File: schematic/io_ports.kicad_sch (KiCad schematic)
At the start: 4 parts, among them J1 Cartridge Port, J2 Expansion Port

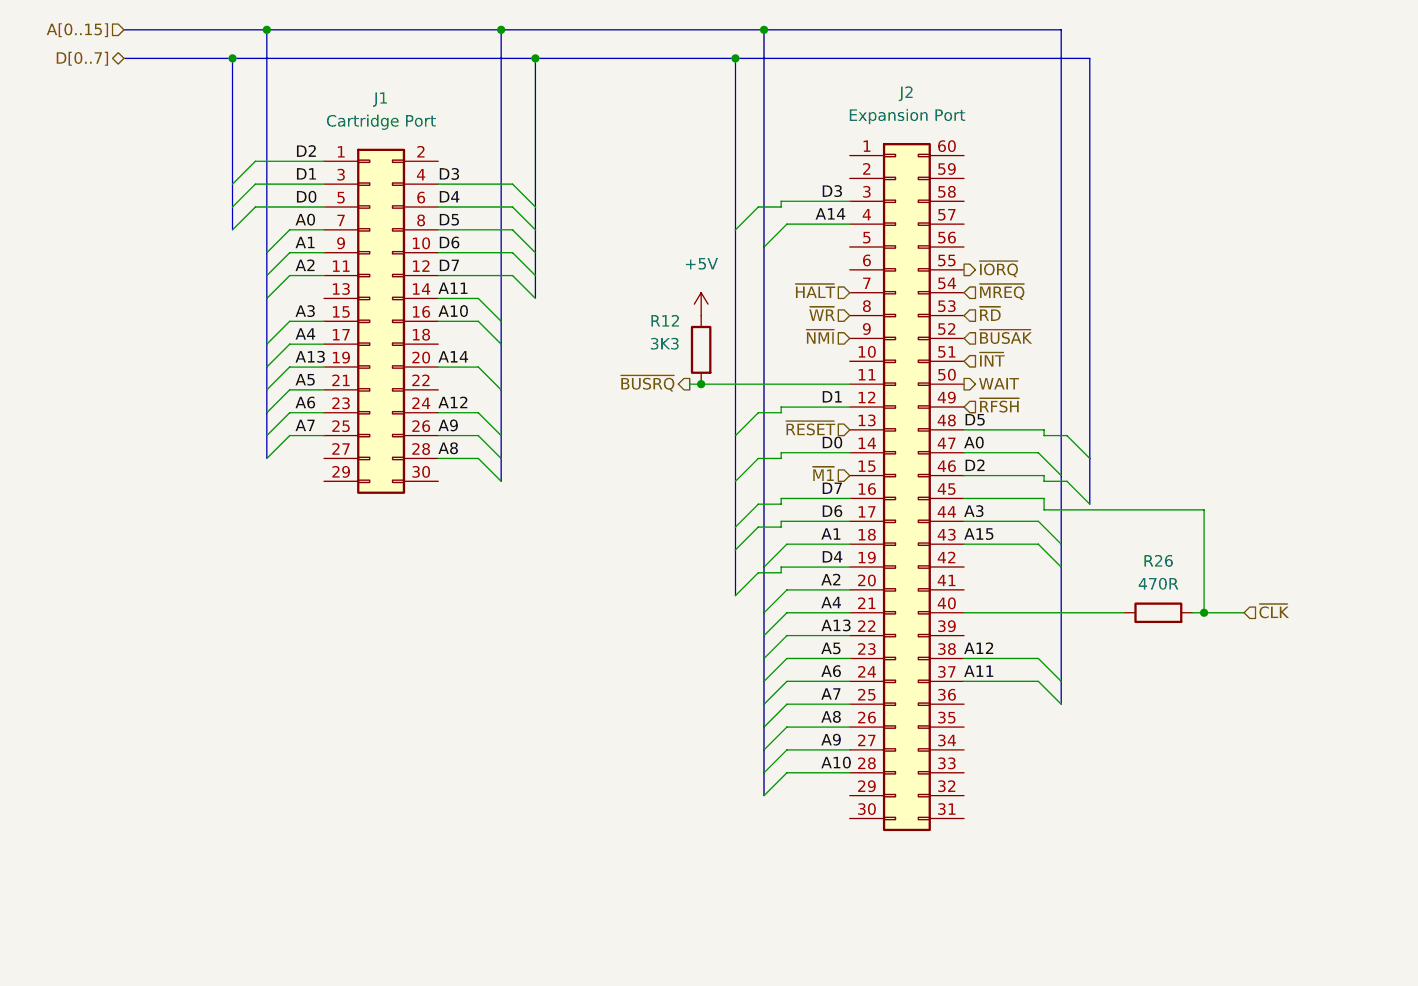
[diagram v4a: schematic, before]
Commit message: added u5 decoder lines, need to rename for chip selects that they actually are in future.
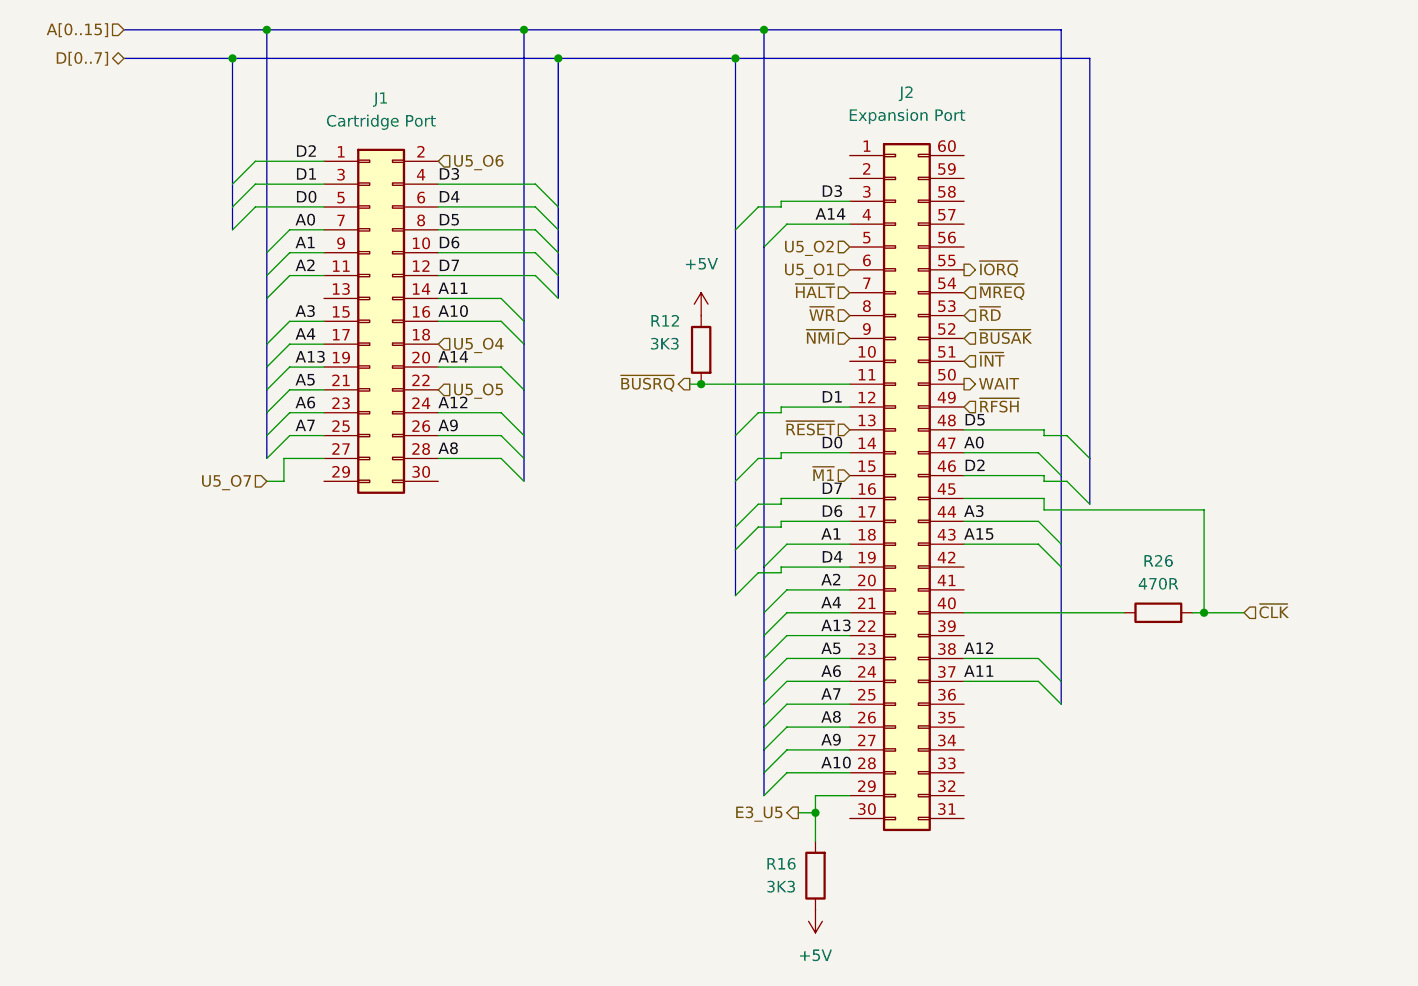
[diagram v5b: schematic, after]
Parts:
- added R16: 3K3, symbol Device:R
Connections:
- net +5V: now also R16.1
- net U5_O4: now reaches J1.18 (Pin_18)
- net U5_O6: now reaches J1.2 (Pin_2)
- net U5_O5: now reaches J1.22 (Pin_22)
- net U5_O7: now reaches J1.27 (Pin_27)
- net E3_U5: now reaches J2.29 (Pin_29)
- net E3_U5: now also R16.2
- net U5_O2: now reaches J2.5 (Pin_5)
- net U5_O1: now reaches J2.6 (Pin_6)

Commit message: added u6 decoder lines, renamed a few lines to make sense to there destination.
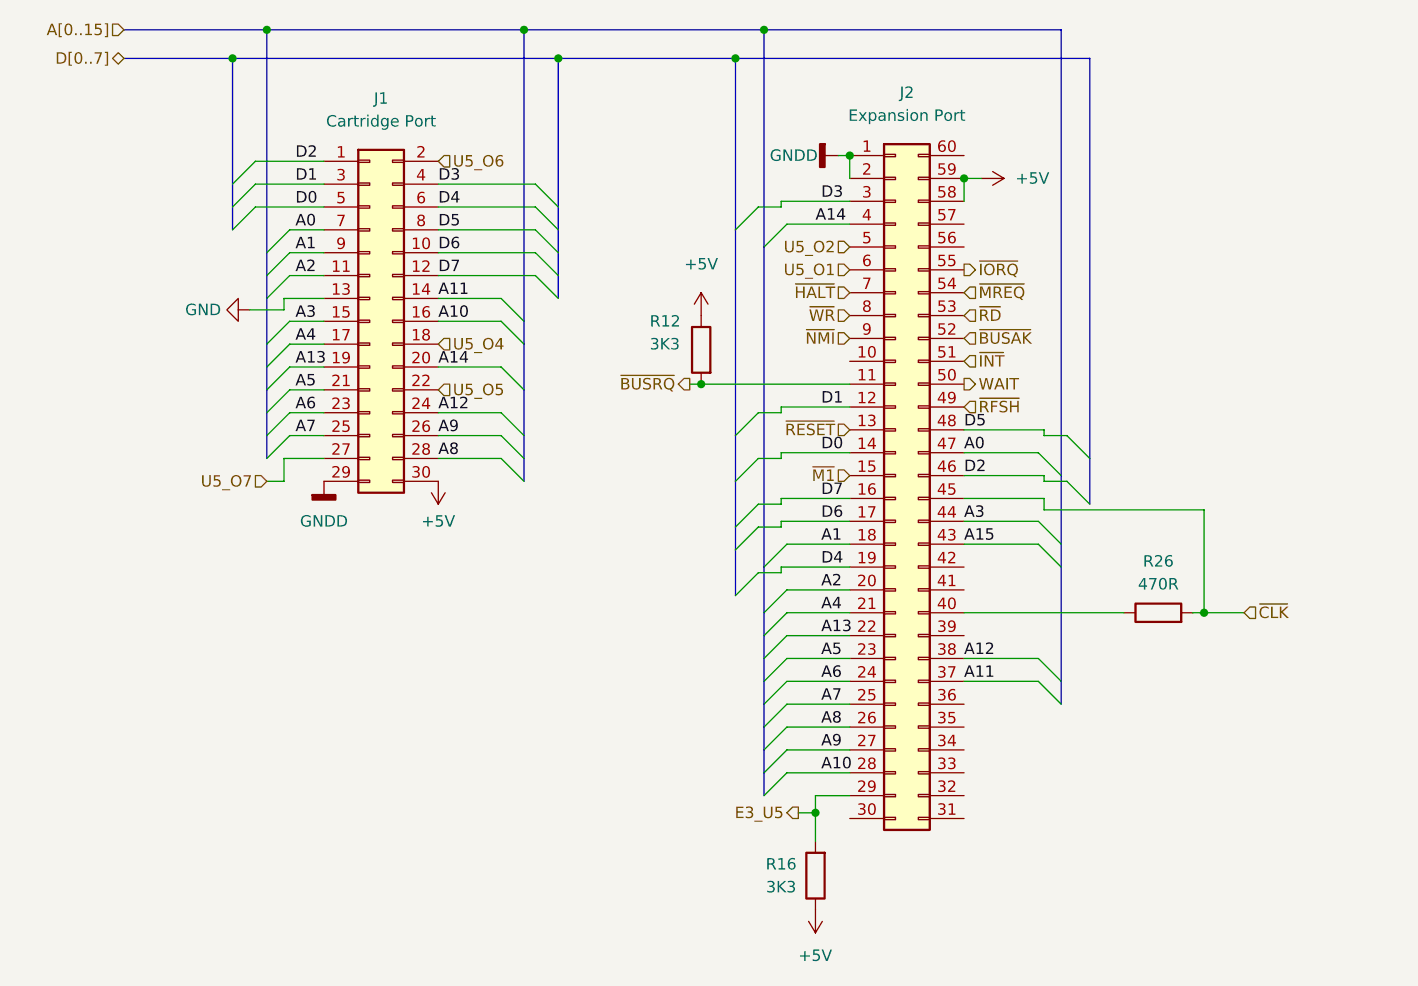
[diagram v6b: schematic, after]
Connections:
- net +5V: now also J1.30 (Pin_30), J2.58 (Pin_58), J2.59 (Pin_59)
- net GND: now reaches J1.13 (Pin_13)
- net GNDD: now reaches J1.29 (Pin_29)
- net GNDD: now also J2.1 (Pin_1), J2.2 (Pin_2)
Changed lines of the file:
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@@
   (junction (at 202.565 97.79) (diameter 0) (color 0 0 0 0)
   )
+  (junction (at 175.895 49.53) (diameter 0) (color 0 0 0 0)
+  )
   (junction (at 153.67 33.02) (diameter 0) (color 0 0 0 0)
   )
@@
   (junction (at 127 33.02) (diameter 0) (color 0 0 0 0)
   )
+  (junction (at 163.195 46.99) (diameter 0) (color 0 0 0 0)
+  )
   (junction (at 159.385 120.015) (diameter 0) (color 0 0 0 0)
   )
@@
     (stroke (width 0) (type default) (color 0 0 0 0))
   )
+  (wire (pts (xy 100.33 62.865) (xy 100.33 64.135))
+    (stroke (width 0) (type default) (color 0 0 0 0))
+  )
   (wire (pts (xy 100.965 57.785) (xy 104.775 57.785))
     (stroke (width 0) (type default) (color 0 0 0 0))
@@
     (stroke (width 0) (type default) (color 0 0 0 0))
   )
+  (wire (pts (xy 175.895 49.53) (xy 175.895 52.07))
+    (stroke (width 0) (type default) (color 0 0 0 0))
+  )
   (wire (pts (xy 163.195 74.93) (xy 155.575 74.93))
     (stroke (width 0) (type default) (color 0 0 0 0))
@@
     (stroke (width 0) (type default) (color 0 0 0 0))
   )
+  (wire (pts (xy 100.33 64.135) (xy 96.52 64.135))
+    (stroke (width 0) (type default) (color 0 0 0 0))
+  )
   (wire (pts (xy 184.785 85.09) (xy 184.785 86.36))
     (stroke (width 0) (type default) (color 0 0 0 0))
@@
     (stroke (width 0) (type default) (color 0 0 0 0))
   )
+  (wire (pts (xy 104.775 62.865) (xy 100.33 62.865))
+    (stroke (width 0) (type default) (color 0 0 0 0))
+  )
   (bus (pts (xy 94.615 36.195) (xy 130.81 36.195))
     (stroke (width 0) (type default) (color 0 0 0 0))
@@
     (stroke (width 0) (type default) (color 0 0 0 0))
   )
+  (wire (pts (xy 161.925 46.99) (xy 163.195 46.99))
+    (stroke (width 0) (type default) (color 0 0 0 0))
+  )
   (bus (pts (xy 153.67 102.87) (xy 153.67 105.41))
     (stroke (width 0) (type default) (color 0 0 0 0))
@@
   )
   (wire (pts (xy 117.475 75.565) (xy 124.46 75.565))
+    (stroke (width 0) (type default) (color 0 0 0 0))
+  )
+  (wire (pts (xy 163.195 46.99) (xy 163.195 49.53))
+    (stroke (width 0) (type default) (color 0 0 0 0))
+  )
+  (wire (pts (xy 175.895 49.53) (xy 177.8 49.53))
     (stroke (width 0) (type default) (color 0 0 0 0))
   )
@@
     (pin "1")
     (pin "2")
+  )
+  (symbol (lib_id "power:+5V") (at 177.8 49.53 270) (unit 1)
+    (in_bom yes) (on_board yes) (fields_autoplaced)
+    (property "Reference" "#PWR?" (id 0) (at 173.99 49.53 0)
+      (effects (font (size 1.27 1.27)) hide)
+    )
+    (property "Value" "+5V" (id 1) (at 181.61 49.5299 90)
+      (effects (font (size 1.27 1.27)) (justify left))
+    )
+    (property "Footprint" "" (id 2) (at 177.8 49.53 0)
+      (effects (font (size 1.27 1.27)) hide)
+    )
+    (property "Datasheet" "" (id 3) (at 177.8 49.53 0)
+      (effects (font (size 1.27 1.27)) hide)
+    )
+    (pin "1")
   )
   (symbol (lib_id "Connector_Generic:Conn_02x30_Counter_Clockwise") (at 168.275 82.55 0) (unit 1)
@@
     (pin "2")
   )
+  (symbol (lib_id "power:+5V") (at 117.475 83.185 180) (unit 1)
+    (in_bom yes) (on_board yes) (fields_autoplaced)
+    (property "Reference" "#PWR?" (id 0) (at 117.475 79.375 0)
+      (effects (font (size 1.27 1.27)) hide)
+    )
+    (property "Value" "+5V" (id 1) (at 117.475 87.63 0))
+    (property "Footprint" "" (id 2) (at 117.475 83.185 0)
+      (effects (font (size 1.27 1.27)) hide)
+    )
+    (property "Datasheet" "" (id 3) (at 117.475 83.185 0)
+      (effects (font (size 1.27 1.27)) hide)
+    )
+    (pin "1")
+  )
+  (symbol (lib_id "power:GNDD") (at 161.925 46.99 270) (unit 1)
+    (in_bom yes) (on_board yes)
+    (property "Reference" "#PWR?" (id 0) (at 155.575 46.99 0)
+      (effects (font (size 1.27 1.27)) hide)
+    )
+    (property "Value" "GNDD" (id 1) (at 154.305 46.99 90)
+      (effects (font (size 1.27 1.27)) (justify left))
+    )
+    (property "Footprint" "" (id 2) (at 161.925 46.99 0)
+      (effects (font (size 1.27 1.27)) hide)
+    )
+    (property "Datasheet" "" (id 3) (at 161.925 46.99 0)
+      (effects (font (size 1.27 1.27)) hide)
+    )
+    (pin "1")
+  )
+  (symbol (lib_id "power:GND") (at 96.52 64.135 270) (unit 1)
+    (in_bom yes) (on_board yes)
+    (property "Reference" "#PWR?" (id 0) (at 90.17 64.135 0)
+      (effects (font (size 1.27 1.27)) hide)
+    )
+    (property "Value" "GND" (id 1) (at 93.345 64.135 90)
+      (effects (font (size 1.27 1.27)) (justify right))
+    )
+    (property "Footprint" "" (id 2) (at 96.52 64.135 0)
+      (effects (font (size 1.27 1.27)) hide)
+    )
+    (property "Datasheet" "" (id 3) (at 96.52 64.135 0)
+      (effects (font (size 1.27 1.27)) hide)
+    )
+    (pin "1")
+  )
+  (symbol (lib_id "power:GNDD") (at 104.775 83.185 0) (unit 1)
+    (in_bom yes) (on_board yes) (fields_autoplaced)
+    (property "Reference" "#PWR?" (id 0) (at 104.775 89.535 0)
+      (effects (font (size 1.27 1.27)) hide)
+    )
+    (property "Value" "GNDD" (id 1) (at 104.775 87.63 0))
+    (property "Footprint" "" (id 2) (at 104.775 83.185 0)
+      (effects (font (size 1.27 1.27)) hide)
+    )
+    (property "Datasheet" "" (id 3) (at 104.775 83.185 0)
+      (effects (font (size 1.27 1.27)) hide)
+    )
+    (pin "1")
+  )
 )

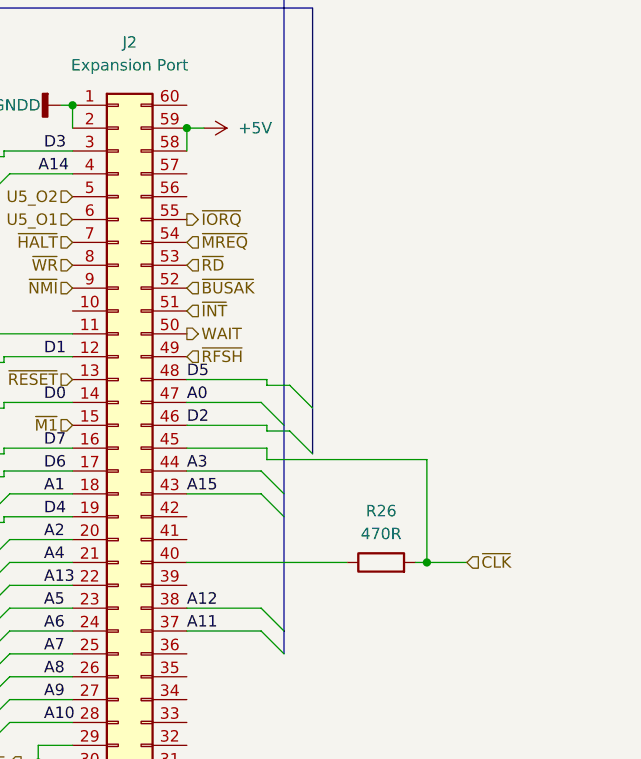
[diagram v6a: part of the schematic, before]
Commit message: completed sound block, finished cart io port, and finished decoder.
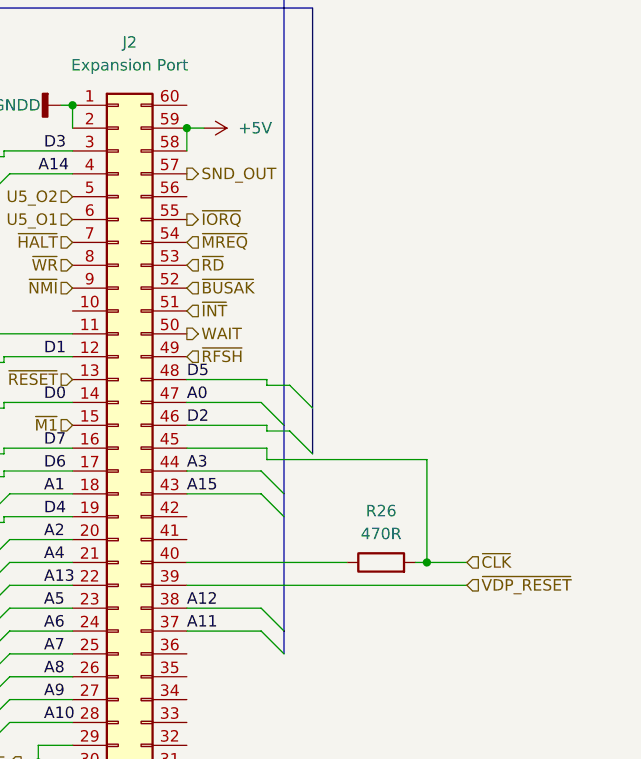
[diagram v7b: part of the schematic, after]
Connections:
- net ~{VDP_RESET}: now reaches J2.39 (Pin_39)
- net SND_OUT: now reaches J2.57 (Pin_57)
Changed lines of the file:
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@@
+    (stroke (width 0) (type default) (color 0 0 0 0))
+  )
+  (wire (pts (xy 207.01 100.33) (xy 175.895 100.33))
     (stroke (width 0) (type default) (color 0 0 0 0))
   )
@@
     (effects (font (size 1.27 1.27)) (justify right))
   )
+  (hierarchical_label "~{VDP_RESET}" (shape input) (at 207.01 100.33 0)
+    (effects (font (size 1.27 1.27)) (justify left))
+  )
   (hierarchical_label "~{HALT}" (shape input) (at 163.195 62.23 180)
     (effects (font (size 1.27 1.27)) (justify right))
@@
     (effects (font (size 1.27 1.27)) (justify left))
   )
+  (hierarchical_label "SND_OUT" (shape output) (at 175.895 54.61 0)
+    (effects (font (size 1.27 1.27)) (justify left))
+  )
